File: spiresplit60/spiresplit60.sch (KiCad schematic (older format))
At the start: 134 parts

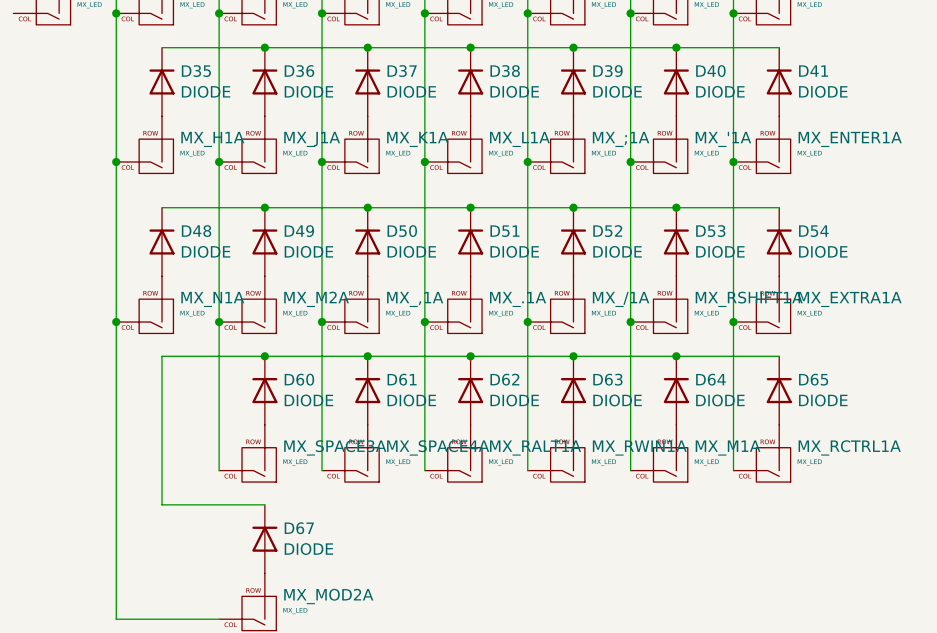
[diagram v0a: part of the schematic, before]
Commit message: Placed all switches and switch diodes
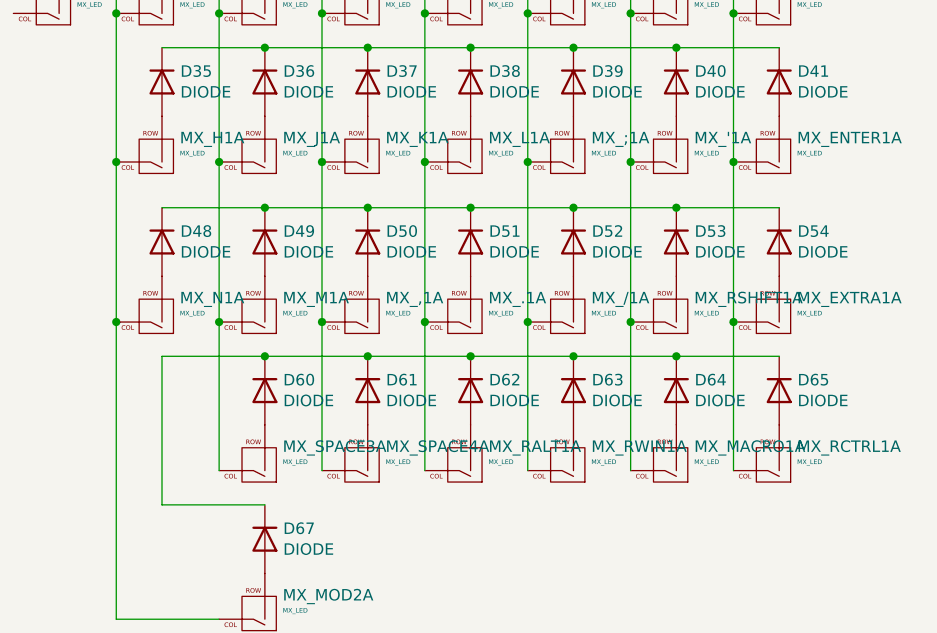
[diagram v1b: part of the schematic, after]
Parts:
- D67: footprint kbd:CherryMX_Choc_1u -> Diode_SMD:D_SOD-123
- renumbered MX_M2 to MX_M1, MX_M1 to MX_MACRO1
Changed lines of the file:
@@
 $EndComp
 $Comp
-L kicad-keyboard-parts:MX_LED MX_M2
+L kicad-keyboard-parts:MX_LED MX_M1
 U 1 1 6329C171
 P 5350 3050
-F 0 "MX_M2" H 5222 2945 50  0000 R CNN
+F 0 "MX_M1" H 5222 2945 50  0000 R CNN
 F 1 "MX_LED" H 5222 3012 20  0000 R CNN
 F 2 "kbd:CherryMX_Choc_1u" H 5400 3150 50  0001 C CNN
@@
 $EndComp
 $Comp
-L kicad-keyboard-parts:MX_LED MX_M1
+L kicad-keyboard-parts:MX_LED MX_MACRO1
 U 1 1 6329C1CB
 P 7150 3700
-F 0 "MX_M1" H 7022 3595 50  0000 R CNN
+F 0 "MX_MACRO1" H 7022 3595 50  0000 R CNN
 F 1 "MX_LED" H 7022 3662 20  0000 R CNN
 F 2 "kbd:CherryMX_Choc_1u" H 7200 3800 50  0001 C CNN
@@
 F 3 "" H 1200 1150 50  0001 C CNN
 	1    1150 1050
-	-1   0    0    1
-$EndComp
-$Comp
-L kicad-keyboard-parts:MX_LED MX_ESC1
-U 1 1 6320F285
-P 700 1050
-F 0 "MX_ESC1" H 572 945 50  0000 R CNN
-F 1 "MX_LED" H 572 1012 20  0000 R CNN
-F 2 "kbd:CherryMX_Choc_1u" H 750 1150 50  0001 C CNN
-F 3 "" H 750 1150 50  0001 C CNN
-	1    700  1050
 	-1   0    0    1
 $EndComp
@@
 F 0 "D67" V 5446 3920 50  0000 R CNN
 F 1 "DIODE" V 5355 3920 50  0000 R CNN
-F 2 "kbd:CherryMX_Choc_1u" H 5400 4000 50  0001 C CNN
+F 2 "Diode_SMD:D_SOD-123" H 5400 4000 50  0001 C CNN
 F 3 "~" H 5400 4000 50  0001 C CNN
 F 4 "Y" H 5400 4000 50  0001 L CNN "Spice_Netlist_Enabled"
@@
 Connection ~ 2550 3200
 Wire Wire Line
-	5400 3200 4950 3200
-Wire Wire Line
 	4950 3200 4950 3850
 Wire Wire Line
@@
 Wire Wire Line
 	5200 2350 5200 1700
-Connection ~ 5200 3050
-Wire Wire Line
-	5200 3050 5200 2350
-Wire Wire Line
-	5200 3700 5200 3050
 Wire Wire Line
 	4750 1050 4750 1700
@@
 	4750 4350 5200 4350
 Connection ~ 4750 3050
+$Comp
+L kicad-keyboard-parts:MX_LED MX_ESC1
+U 1 1 6320F285
+P 700 1050
+F 0 "MX_ESC1" H 572 945 50  0000 R CNN
+F 1 "MX_LED" H 572 1012 20  0000 R CNN
+F 2 "kbd:CherryMX_Choc_1u" H 750 1150 50  0001 C CNN
+F 3 "" H 750 1150 50  0001 C CNN
+	1    700  1050
+	-1   0    0    1
+$EndComp
+Wire Wire Line
+	5200 2350 5200 3050
+Connection ~ 5200 3050
+Wire Wire Line
+	5200 3050 5200 3700
+Wire Wire Line
+	4950 3200 5400 3200
 $EndSCHEMATC

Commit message: idek what is going on with the lib
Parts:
- added J? (x2): AudioJack4, symbol Connector:AudioJack4
- added SW1, SW2: SW_Push, Button_Switch_SMD:SW_SPST_TL3342, symbol Switch:SW_Push
- added U1, U2: ProMicro, kbd:ProMicro_v3, symbol kbd:ProMicro
- MX_'1, MX_,1, MX_-1, MX_.1, MX_/1, MX_0, MX_1, MX_2, MX_3, MX_4, MX_5, MX_6, MX_7, MX_8, MX_9, MX_;1, MX_=1, MX_A1, MX_B1, MX_BS1, MX_C1, MX_CAPS1, MX_D1, MX_E1, MX_ENTER1, MX_ESC1, MX_EXTRA1, MX_F1, MX_G1, MX_H1, MX_I1, MX_J1, MX_K1, MX_L1, MX_LALT1, MX_LCTRL1, MX_LSHIFT1, MX_LWIN1, MX_M1, MX_MACRO1, MX_MOD1, MX_MOD2, MX_N1, MX_O1, MX_P1, MX_Q1, MX_R1, MX_RALT1, MX_RCTRL1, MX_RSHIFT1, MX_RWIN1, MX_S1, MX_SPACE1, MX_SPACE2, MX_SPACE3, MX_SPACE4, MX_T1, MX_TAB1, MX_U1, MX_V1, MX_W1, MX_X1, MX_Y1, MX_Z1, MX_[1, MX_\1, MX_]1: footprint kbd:CherryMX_Choc_1u -> keyswitches:SW_PG1350
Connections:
- net at MX_A1.1 (COL), MX_Q1.1 (COL), MX_Z1.1 (COL): now also MX_2.1 (COL), MX_LALT1.1 (COL); no longer MX_1.1 (COL), MX_LWIN1.1 (COL)
- net at MX_S1.1 (COL), MX_W1.1 (COL), MX_X1.1 (COL): now also MX_3.1 (COL); no longer MX_2.1 (COL), MX_LALT1.1 (COL)
- net at MX_C1.1 (COL), MX_D1.1 (COL), MX_E1.1 (COL)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: now also MX_4.1 (COL); no longer MX_3.1 (COL)
- net at MX_F1.1 (COL), MX_R1.1 (COL), MX_SPACE2.1 (COL)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: now also MX_5.1 (COL); no longer MX_4.1 (COL)
- net at MX_B1.1 (COL), MX_G1.1 (COL), MX_MOD1.1 (COL)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: now also MX_6.1 (COL); no longer MX_5.1 (COL)
- net at MX_7.1 (COL), MX_H1.1 (COL), MX_N1.1 (COL): now also MX_SPACE3.1 (COL), MX_Y1.1 (COL); no longer MX_MOD2.1 (COL), MX_U1.1 (COL)
- net at MX_8.1 (COL), MX_J1.1 (COL), MX_M1.1 (COL): now also MX_MOD2.1 (COL), MX_U1.1 (COL); no longer MX_I1.1 (COL), MX_SPACE3.1 (COL)
- net at MX_,1.1 (COL), MX_9.1 (COL), MX_K1.1 (COL)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: now also MX_I1.1 (COL); no longer MX_O1.1 (COL)
- net at MX_.1.1 (COL), MX_0.1 (COL), MX_L1.1 (COL)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: now also MX_O1.1 (COL); no longer MX_P1.1 (COL)
- net at MX_-1.1 (COL), MX_/1.1 (COL), MX_;1.1 (COL)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: now also MX_P1.1 (COL); no longer MX_[1.1 (COL)
- net at MX_MACRO1.1 (COL), MX_RSHIFT1.1 (COL), MX_]1.1 (COL): no longer MX_'1.1 (COL), MX_=1.1 (COL)
- net Col1: now reaches D1.2 (K), D2.2 (K), D3.2 (K), D4.2 (K), D5.2 (K), D6.2 (K), D7.2 (K)
- net Col10: now reaches D10.2 (K), D11.2 (K), D12.2 (K), D13.2 (K), D14.2 (K), D8.2 (K), D9.2 (K)
- net Row2: now reaches D15.2 (K), D16.2 (K), D17.2 (K), D18.2 (K), D19.2 (K)
- net Row2: no longer D20.2 (K)
- net Row3: now reaches D29.2 (K), D30.2 (K), D31.2 (K), D32.2 (K), D33.2 (K), D34.2 (K)
- net Row4: now reaches D42.2 (K), D43.2 (K), D44.2 (K), D45.2 (K), D46.2 (K), D47.2 (K)
- net Row5: now reaches D55.2 (K), D56.2 (K), D57.2 (K), D58.2 (K), D59.2 (K), D66.2 (K)
- net Col14: now reaches D21.2 (K), D22.2 (K), D23.2 (K), D24.2 (K), D25.2 (K), D26.2 (K), D27.2 (K), D28.2 (K)
- net Row8: now reaches D35.2 (K), D36.2 (K), D37.2 (K), D38.2 (K), D39.2 (K), D40.2 (K), D41.2 (K)
- net Row9: now reaches D48.2 (K), D49.2 (K), D50.2 (K), D51.2 (K), D52.2 (K), D53.2 (K), D54.2 (K)
- net Row10: now reaches D60.2 (K), D61.2 (K), D62.2 (K), D63.2 (K), D64.2 (K), D65.2 (K), D67.2 (K)
- new net: MX_1.1 (COL), MX_LWIN1.1 (COL)
- new net: MX_'1.1 (COL), MX_=1.1 (COL), MX_[1.1 (COL)
- new net +5V: J?.R2, J?.R2, U1.21 (VCC), U2.21 (VCC)
- new net GND: J?.S, J?.S, SW1.1, SW2.1, U1.23 (GND), U1.3 (GND), U1.4 (GND), U2.23 (GND), U2.3 (GND), U2.4 (GND)
- new net RST1: SW2.2, U2.22 (RST)
- new net RST2: SW1.2, U1.22 (RST)
- new net Serial1: J?.R1, U2.5 (2/D1/SDA)
- new net Serial2: J?.R1, U1.5 (2/D1/SDA)
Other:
- moved on the sheet: D1, D10, D11, D12, D13, D14, D15, D16, D17, D18, D19, D2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

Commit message: Finished edge cuts
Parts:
- removed J? (x2): AudioJack4, symbol Connector:AudioJack4
- added U3, U4: TRRS, Keebio-Parts:TRRS-PJ-320A, symbol keebio:TRRS
- MX_'1, MX_,1, MX_-1, MX_.1, MX_/1, MX_0, MX_1, MX_2, MX_3, MX_4, MX_5, MX_6, MX_7, MX_8, MX_9, MX_;1, MX_=1, MX_A1, MX_B1, MX_BS1, MX_C1, MX_CAPS1, MX_D1, MX_E1, MX_ENTER1, MX_ESC1, MX_EXTRA1, MX_F1, MX_G1, MX_H1, MX_I1, MX_J1, MX_K1, MX_L1, MX_LALT1, MX_LCTRL1, MX_LSHIFT1, MX_LWIN1, MX_M1, MX_MACRO1, MX_MOD1, MX_MOD2, MX_N1, MX_O1, MX_P1, MX_Q1, MX_R1, MX_RALT1, MX_RCTRL1, MX_RSHIFT1, MX_RWIN1, MX_S1, MX_SPACE1, MX_SPACE2, MX_SPACE3, MX_SPACE4, MX_T1, MX_TAB1, MX_U1, MX_V1, MX_W1, MX_X1, MX_Y1, MX_Z1, MX_[1, MX_\1, MX_]1: footprint keyswitches:SW_PG1350 -> Keebio-Parts:Kailh-PG1350-1u; symbol kicad-keyboard-parts:MX_LED -> spiresplit60-rescue:MX_LED-kicad-keyboard-parts
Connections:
- net +5V: now also U3.4 (RING2), U4.4 (RING2)
- net GND: now also U3.1 (SLEEVE), U4.1 (SLEEVE)
- net Serial1: now also U4.3 (RING1)
- net Serial2: now also U3.3 (RING1)
